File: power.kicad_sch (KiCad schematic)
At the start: 6 parts, among them U50 LDL1117S33R, U52 MIC5219-2.85YM5-TR

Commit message: moving along
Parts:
- added C121, C125: 100nF, Capacitor_SMD:C_0603_1608Metric, symbol Capacitors:0603_nf100
- added C123, C124, C134: 1uF, Capacitor_SMD:C_0603_1608Metric, symbol Capacitors:0603_uF001_50V
- added C126, C127, C128, C130, C132, C133: 10uF, Capacitor_SMD:C_1206_3216Metric, symbol Capacitors:1206_uF010
- added C141, C142, C144, C146: 47uF, Capacitor_SMD:C_1206_3216Metric, symbol Capacitors:1206_uF010
- added L4: IHLP6767GZERR47M11, Inductors:IND_IHLP-6767GZ_VIS, symbol Inductors:IHLP6767GZERR47M11
- added R46: 10K, Resistor_SMD:R_0603_1608Metric, symbol Resistors:0603_R_10K
- added R47: 73.2K, Resistor_SMD:R_0603_1608Metric, symbol Resistors:0603_R_73K2
- added R49: 24.9k, Resistor_SMD:R_0603_1608Metric, symbol Resistors:0603_R_52K3
- added R50, R51: x, Resistor_SMD:R_0603_1608Metric, symbol Resistors:0603_R_52K3
- added U55: TPS548D26RXXR, DCDC:WQFN_C26RXXR_TEX, symbol DCDC:TPS548C26RXXR
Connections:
- net +12V: now also C125.1, C126.1, C127.1, C128.1, C130.1, C132.1, C133.1, U55.20 (PVIN), U55.21 (PVIN), U55.22 (PVIN), U55.23 (PVIN), U55.24 (PVIN), U55.3 (AVIN)
- net 5V_LP: now also C123.1, C124.1, U55.27 (EN), U55.5 (VDRV)
- net GND: now also C123.2, C124.2, C125.2, C126.2, C127.2, C128.2, C130.2, C132.2, C133.2, C134.2, C141.2, C142.2, C144.2, C146.2, R46.2, R49.2, R50.2, R51.2, U55.10 (PGND), U55.19 (PGND), U55.31 (GOSNS), U55.32 (AGND), U55.7 (PGND), U55.8 (PGND), U55.9 (PGND)
- new net: R50.1, U55.36 (MODE)
- new net: R49.1, U55.1 (ILIM)
- new net: R46.1, R47.1, U55.30 (FB)
- new net: L4.1, U55.11 (SW), U55.12 (SW), U55.13 (SW), U55.14 (SW), U55.15 (SW), U55.16 (SW), U55.17 (SW), U55.18 (SW)
- new net: C121.2, U55.25 (PHASE)
- new net: C121.1, U55.26 (BOOT)
- new net: R51.1, U55.29 (SS)
- new net +5V: C134.1, C141.1, C142.1, C144.1, C146.1, L4.2, R47.2, U55.28 (VOSNS)
- no-connect marks 0 -> 1
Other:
- removed sheet DCDC_30A

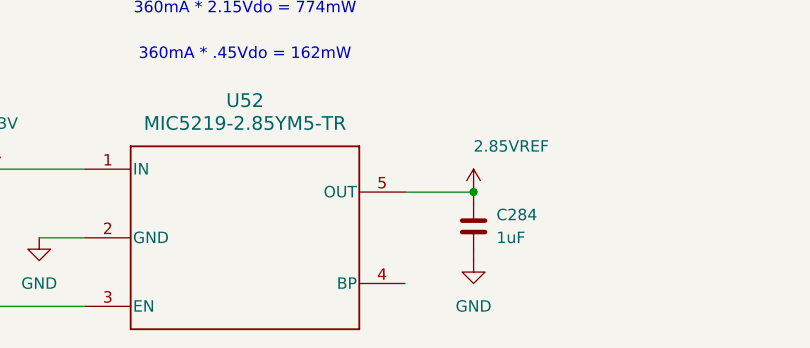
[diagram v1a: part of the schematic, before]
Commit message: 6 layers now
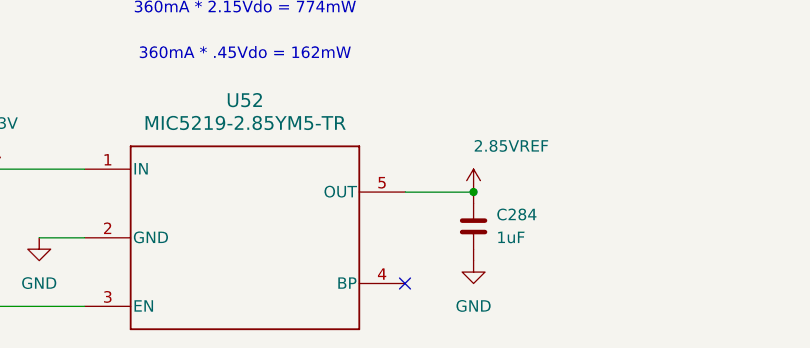
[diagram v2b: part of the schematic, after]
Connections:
- no-connect marks 1 -> 2
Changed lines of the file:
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@@
+	)
+	(no_connect
+		(at 83.82 124.46)
 	)
 	(no_connect

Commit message: june_26
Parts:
- removed C121, C125: 100nF, Capacitor_SMD:C_0603_1608Metric, symbol Capacitors:0603_nf100
- removed C141, C142, C144, C146: 47uF, Capacitor_SMD:C_1206_3216Metric, symbol Capacitors:1206_uF010
- removed R47: 73.2K, Resistor_SMD:R_0603_1608Metric, symbol Resistors:0603_R_73K2
- added C121, C125: 100nF, Capacitor_SMD:C_0402_1005Metric, symbol Capacitors:0402_nF100_50V
- added C141: 1uF, Capacitor_SMD:C_0603_1608Metric, symbol Capacitors:0603_uF001_50V
- added C179, C180, C184: 100uF, Pulsemedica_Capacitors:WCAP-ASLI_6.3X7.7_DXL_, symbol Pulsemedica_Capacitors:WCAP-ASLI_6.3X7.7
- added C186, C188, C189, C190, C191, C193: 10uF, Capacitor_SMD:C_1206_3216Metric, symbol Capacitors:1206_uF010
- added C281: 1nF, Capacitor_SMD:C_0402_1005Metric, symbol Capacitors:0402_nF1_50V
- added D8: LTST-C230KGKT, LED_SMD:LED_1206_3216Metric, symbol LED:IR26-21C_L110_TR8
- added R47: 75k, Resistor_SMD:R_0603_1608Metric, symbol Resistors:0603_R_75k
- added R55, R68, R69: 1, Resistor_SMD:R_0603_1608Metric, symbol Resistors:0603_R001
- added R70, R71: 10K, Resistor_SMD:R_0603_1608Metric, symbol Resistors:0603_R_10K
- added R73: 1k, Resistor_SMD:R_0603_1608Metric, symbol Resistors:0603_R_01K
- C127: price .39 -> .388
- R46: DN (none) -> P10KDBCT-ND; MFR (none) -> Panasonic Industry; MPN (none) -> ERA-3AEB103V; price (none) -> .1
- R49: symbol Resistors:0603_R_52K3 -> Resistors:0603_R_24K9; MFR Panasonic Electronic Components -> Panasonic Industry; MPN P24.9KDBCT-ND -> ERA-3AEB2492V
- U50: cost .45 -> (none); price (none) -> .45
- U52: price (none) -> 2
- U55: DN MOUSER -> 296-TPS548D26RXXRCT-ND; MPN TPS548C26RXXR -> TPS548D26RXXR; Price 8.93 -> (none); alernate (none) -> TPS548C26 (different Vfb); price (none) -> 9.21
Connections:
- net +12V: now also C125.1, C179.1; no longer U55.3 (AVIN)
- net +5V: now also C180.1, C184.1, C186.1, C188.1, C189.1, C190.1, C191.1, C193.1, R68.1, R73.1; no longer U55.28 (VOSNS)
- net 5V_LP: now also C141.1, R55.1, R70.2; no longer C123.1, U55.27 (EN)
- net GND: now also U55.33 (NC/GND), U55.34 (NC/GND), U55.35 (NC/GND), C125.2, C141.2, C179.2, C180.2, C184.2, C186.2, C188.2, C189.2, C190.2, C191.2, C193.2, D8.1 (K), R69.2, R71.2; no longer R46.2, U55.31 (GOSNS)
- net at R46.1, U55.30 (FB): now also C281.1, R47.1
- net at U55.2 (PG): now also D8.2 (A), R73.2
- net at U55.25 (PHASE): now also C121.2
- net at U55.26 (BOOT): now also C121.1
- net at U55.4 (VCC): now also C123.1, U55.3 (AVIN), R55.2
- new net: C281.2, R47.2, R68.2, U55.28 (VOSNS)
- new net: R46.2, R69.1, U55.31 (GOSNS)
- new net DCDC EN: R70.1, R71.1, U55.27 (EN)
- no-connect marks 2 -> 3
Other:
- note added: "+40uF"
- note added: "1+44+88 uF"
- note added: "10 mA max on PG"
- note added: "12V"
- note added: "16.6A"
- note added: "180mA"
- note added: "200mA"
- note added: "2V85"
- note added: "360mA"
- note added: "3V3"
- note added: "40A"
- note added: "5V"
- note added: "5V_LP"
- moved on the sheet: C124, C134
